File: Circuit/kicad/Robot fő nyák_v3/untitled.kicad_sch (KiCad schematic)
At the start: 4 parts, among them J13 Conn_01x06_Socket, J36 Conn_01x06_Socket, J37 Conn_01x06_Socket, J38 Conn_01x06_Socket

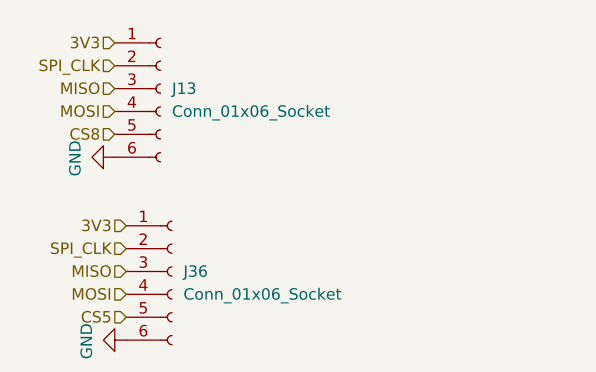
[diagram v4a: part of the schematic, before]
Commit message: kicad v0.1 footprint- assing spi finish
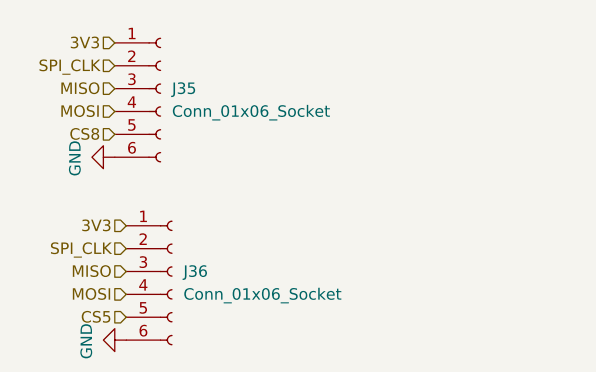
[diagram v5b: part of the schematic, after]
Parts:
- J35: renamed from J13; footprint (none) -> Connector_JST:JST_PH_B6B-PH-K_1x06_P2.00mm_Vertical
- J36, J37, J38: footprint (none) -> Connector_JST:JST_PH_B6B-PH-K_1x06_P2.00mm_Vertical
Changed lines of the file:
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@@
 			)
 		)
-		(property "Footprint" ""
+		(property "Footprint" "Connector_JST:JST_PH_B6B-PH-K_1x06_P2.00mm_Vertical"
 			(at 44.45 85.09 0)
 			(effects
@@
 		(on_board yes)
 		(dnp no)
-		(property "Reference" "#PWR016"
+		(property "Reference" "#PWR0124"
 			(at 33.02 92.71 0)
 			(effects
@@
 			(project "CM5IO"
 				(path "/e63e39d7-6ac0-4ffd-8aa3-1841a4541b55/a83afe30-5c7e-43cb-a5b2-f6f97a0812b3/86209e6a-92ae-4699-a125-02d46b525fc7"
-					(reference "#PWR016")
+					(reference "#PWR0124")
 					(unit 1)
 				)
@@
 		(on_board yes)
 		(dnp no)
-		(property "Reference" "#PWR015"
+		(property "Reference" "#PWR0123"
 			(at 31.75 73.66 0)
 			(effects
@@
 			(project "CM5IO"
 				(path "/e63e39d7-6ac0-4ffd-8aa3-1841a4541b55/a83afe30-5c7e-43cb-a5b2-f6f97a0812b3/86209e6a-92ae-4699-a125-02d46b525fc7"
-					(reference "#PWR015")
+					(reference "#PWR0123")
 					(unit 1)
 				)
@@
 			)
 		)
-		(property "Footprint" ""
+		(property "Footprint" "Connector_JST:JST_PH_B6B-PH-K_1x06_P2.00mm_Vertical"
 			(at 43.18 66.04 0)
 			(effects
@@
 			)
 		)
-		(property "Footprint" ""
+		(property "Footprint" "Connector_JST:JST_PH_B6B-PH-K_1x06_P2.00mm_Vertical"
 			(at 43.18 44.45 0)
 			(effects
@@
 		(dnp no)
 		(fields_autoplaced yes)
-		(property "Reference" "J13"
+		(property "Reference" "J35"
 			(at 43.18 24.1299 0)
 			(effects
@@
 			)
 		)
-		(property "Footprint" ""
+		(property "Footprint" "Connector_JST:JST_PH_B6B-PH-K_1x06_P2.00mm_Vertical"
 			(at 41.91 24.13 0)
 			(effects
@@
 			(project ""
 				(path "/e63e39d7-6ac0-4ffd-8aa3-1841a4541b55/a83afe30-5c7e-43cb-a5b2-f6f97a0812b3/86209e6a-92ae-4699-a125-02d46b525fc7"
-					(reference "J13")
+					(reference "J35")
 					(unit 1)
 				)
@@
 		(on_board yes)
 		(dnp no)
-		(property "Reference" "#PWR08"
+		(property "Reference" "#PWR0121"
 			(at 30.48 31.75 0)
 			(effects
@@
 			(project "CM5IO"
 				(path "/e63e39d7-6ac0-4ffd-8aa3-1841a4541b55/a83afe30-5c7e-43cb-a5b2-f6f97a0812b3/86209e6a-92ae-4699-a125-02d46b525fc7"
-					(reference "#PWR08")
+					(reference "#PWR0121")
 					(unit 1)
 				)
@@
 		(on_board yes)
 		(dnp no)
-		(property "Reference" "#PWR014"
+		(property "Reference" "#PWR0122"
 			(at 31.75 52.07 0)
 			(effects
@@
 			(project "CM5IO"
 				(path "/e63e39d7-6ac0-4ffd-8aa3-1841a4541b55/a83afe30-5c7e-43cb-a5b2-f6f97a0812b3/86209e6a-92ae-4699-a125-02d46b525fc7"
-					(reference "#PWR014")
-					(unit 1)
-				)
+					(reference "#PWR0122")
+					(unit 1)
+				)

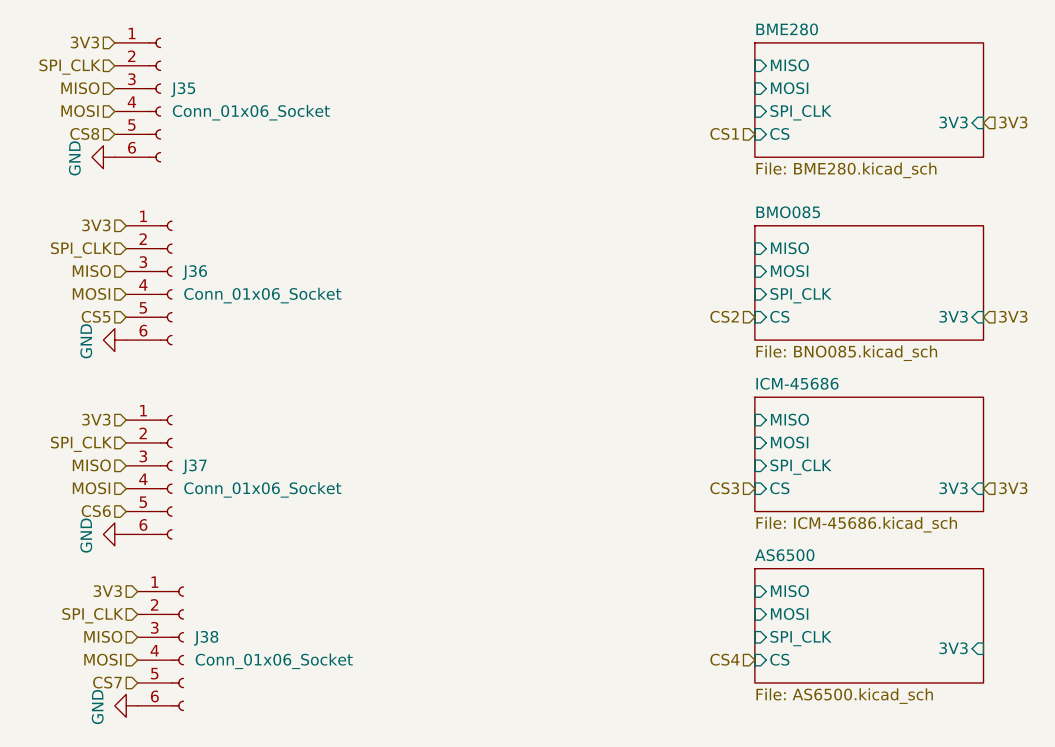
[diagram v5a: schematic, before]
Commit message: kicad  i2c and spi mux fixed and bugfixs
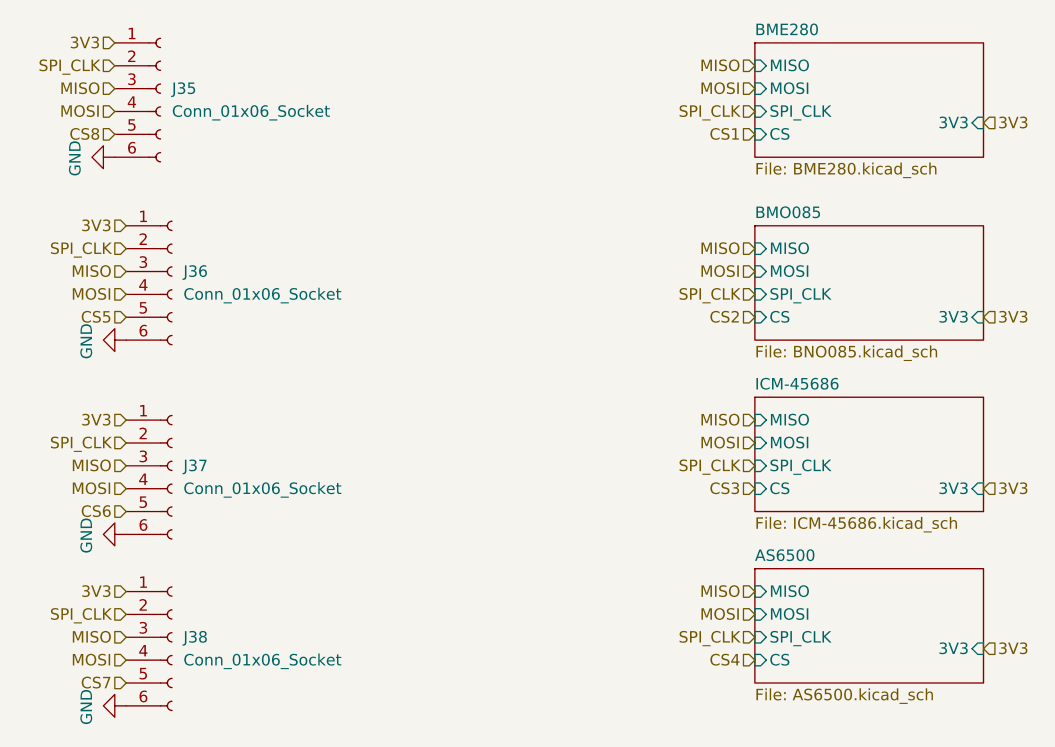
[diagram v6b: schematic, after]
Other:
- moved on the sheet: J38
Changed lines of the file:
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@@
 	(hierarchical_label "SPI_CLK"
 		(shape input)
-		(at 39.37 82.55 180)
+		(at 107.95 66.04 180)
+		(effects
+			(font
+				(size 1.27 1.27)
+			)
+			(justify right)
+		)
+	)
+	(hierarchical_label "MISO"
+		(shape input)
+		(at 107.95 60.96 180)
+		(effects
+			(font
+				(size 1.27 1.27)
+			)
+			(justify right)
+		)
+	)
+	(hierarchical_label "MOSI"
+		(shape input)
+		(at 107.95 63.5 180)
+		(effects
+			(font
+				(size 1.27 1.27)
+			)
+			(justify right)
+		)
+	)
+	(hierarchical_label "SPI_CLK"
+		(shape input)
+		(at 38.1 82.55 180)
 		(effects
 			(font
@@
 		)
 	)
+	(hierarchical_label "SPI_CLK"
+		(shape input)
+		(at 107.95 26.67 180)
+		(effects
+			(font
+				(size 1.27 1.27)
+			)
+			(justify right)
+		)
+	)
 	(hierarchical_label "MISO"
 		(shape input)
@@
 	(hierarchical_label "3V3"
 		(shape input)
+		(at 133.35 86.36 0)
+		(effects
+			(font
+				(size 1.27 1.27)
+			)
+			(justify left)
+		)
+	)
+	(hierarchical_label "3V3"
+		(shape input)
 		(at 133.35 68.58 0)
 		(effects
@@
 	(hierarchical_label "CS7"
 		(shape input)
-		(at 39.37 90.17 180)
+		(at 38.1 90.17 180)
+		(effects
+			(font
+				(size 1.27 1.27)
+			)
+			(justify right)
+		)
+	)
+	(hierarchical_label "SPI_CLK"
+		(shape input)
+		(at 107.95 46.99 180)
 		(effects
 			(font
@@
 		)
 	)
+	(hierarchical_label "MOSI"
+		(shape input)
+		(at 107.95 82.55 180)
+		(effects
+			(font
+				(size 1.27 1.27)
+			)
+			(justify right)
+		)
+	)
 	(hierarchical_label "CS1"
 		(shape input)
@@
 		)
 	)
+	(hierarchical_label "MISO"
+		(shape input)
+		(at 107.95 80.01 180)
+		(effects
+			(font
+				(size 1.27 1.27)
+			)
+			(justify right)
+		)
+	)
 	(hierarchical_label "CS8"
 		(shape input)
@@
 	(hierarchical_label "MISO"
 		(shape input)
-		(at 39.37 85.09 180)
+		(at 38.1 85.09 180)
 		(effects
 			(font
@@
 		)
 	)
+	(hierarchical_label "MOSI"
+		(shape input)
+		(at 107.95 44.45 180)
+		(effects
+			(font
+				(size 1.27 1.27)
+			)
+			(justify right)
+		)
+	)
+	(hierarchical_label "SPI_CLK"
+		(shape input)
+		(at 107.95 85.09 180)
+		(effects
+			(font
+				(size 1.27 1.27)
+			)
+			(justify right)
+		)
+	)
+	(hierarchical_label "MOSI"
+		(shape input)
+		(at 107.95 24.13 180)
+		(effects
+			(font
+				(size 1.27 1.27)
+			)
+			(justify right)
+		)
+	)
 	(hierarchical_label "3V3"
 		(shape input)
@@
 	(hierarchical_label "MISO"
 		(shape input)
+		(at 107.95 41.91 180)
+		(effects
+			(font
+				(size 1.27 1.27)
+			)
+			(justify right)
+		)
+	)
+	(hierarchical_label "MISO"
+		(shape input)
 		(at 38.1 44.45 180)
 		(effects
@@
 		)
 	)
+	(hierarchical_label "MISO"
+		(shape input)
+		(at 107.95 21.59 180)
+		(effects
+			(font
+				(size 1.27 1.27)
+			)
+			(justify right)
+		)
+	)
 	(hierarchical_label "SPI_CLK"
 		(shape input)
@@
 	(hierarchical_label "3V3"
 		(shape input)
-		(at 39.37 80.01 180)
-		(effects
-			(font
-				(size 1.27 1.27)
-			)
-			(justify right)
-		)
-	)
-	(hierarchical_label "MOSI"
-		(shape input)
-		(at 39.37 87.63 180)
+		(at 38.1 80.01 180)
+		(effects
+			(font
+				(size 1.27 1.27)
+			)
+			(justify right)
+		)
+	)
+	(hierarchical_label "MOSI"
+		(shape input)
+		(at 38.1 87.63 180)
 		(effects
 			(font
@@
 	(symbol
 		(lib_id "Connector:Conn_01x06_Socket")
-		(at 44.45 85.09 0)
+		(at 43.18 85.09 0)
 		(unit 1)
 		(exclude_from_sim no)
@@
 		(fields_autoplaced yes)
 		(property "Reference" "J38"
-			(at 45.72 85.0899 0)
+			(at 44.45 85.0899 0)
 			(effects
 				(font
@@
 		)
 		(property "Value" "Conn_01x06_Socket"
-			(at 45.72 87.6299 0)
+			(at 44.45 87.6299 0)
 			(effects
 				(font
@@
 		)
 		(property "Footprint" "Connector_JST:JST_PH_B6B-PH-K_1x06_P2.00mm_Vertical"
-			(at 44.45 85.09 0)
+			(at 43.18 85.09 0)
 			(effects
 				(font
@@
 		)
 		(property "Datasheet" "~"
-			(at 44.45 85.09 0)
+			(at 43.18 85.09 0)
 			(effects
 				(font
@@
 		)
 		(property "Description" "Generic connector, single row, 01x06, script generated"
-			(at 44.45 85.09 0)
+			(at 43.18 85.09 0)
 			(effects
 				(font
@@
 	(symbol
 		(lib_id "power:GND")
-		(at 39.37 92.71 270)
+		(at 38.1 92.71 270)
 		(unit 1)
 		(exclude_from_sim no)
@@
 		(dnp no)
 		(property "Reference" "#PWR0124"
-			(at 33.02 92.71 0)
+			(at 31.75 92.71 0)
 			(effects
 				(font
@@
 		)
 		(property "Value" "GND"
-			(at 34.9758 92.837 0)
+			(at 33.7058 92.837 0)
 			(effects
 				(font
@@
 		)
 		(property "Footprint" ""
-			(at 39.37 92.71 0)
+			(at 38.1 92.71 0)
 			(effects
 				(font
@@
 		)
 		(property "Datasheet" ""
-			(at 39.37 92.71 0)
+			(at 38.1 92.71 0)
 			(effects
 				(font
@@
 		)
 		(property "Description" "Power symbol creates a global label with name \"GND\" , ground"
-			(at 39.37 92.71 0)
-			(effects
-				(font
+			(at 38.1 92.71 0)
+			(effects
+				(font

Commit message: kicad update new readme media updates the circuit is 95% finished
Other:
- added sheet ADS8688 (ADS8688 .kicad_sch)
- moved on the sheet: J35, J36, J37, J38

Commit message: readme updated kicad circuit V1
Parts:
- renumbered J35 to SPI1, J38 to SPI2, J37 to SPI3, J36 to SPI4
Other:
- removed sheet AS6500
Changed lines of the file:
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@@
 		(dnp no)
 		(fields_autoplaced yes)
-		(property "Reference" "J38"
+		(property "Reference" "SPI2"
 			(at 44.45 46.9899 0)
 			(effects
@@
 			(project "CM5IO"
 				(path "/e63e39d7-6ac0-4ffd-8aa3-1841a4541b55/a83afe30-5c7e-43cb-a5b2-f6f97a0812b3/86209e6a-92ae-4699-a125-02d46b525fc7"
-					(reference "J38")
+					(reference "SPI2")
 					(unit 1)
 				)
@@
 		(on_board yes)
 		(dnp no)
-		(property "Reference" "#PWR0124"
+		(property "Reference" "#PWR0143"
 			(at 31.75 54.61 0)
 			(effects
@@
 			(project "CM5IO"
 				(path "/e63e39d7-6ac0-4ffd-8aa3-1841a4541b55/a83afe30-5c7e-43cb-a5b2-f6f97a0812b3/86209e6a-92ae-4699-a125-02d46b525fc7"
-					(reference "#PWR0124")
+					(reference "#PWR0143")
 					(unit 1)
 				)
@@
 		(on_board yes)
 		(dnp no)
-		(property "Reference" "#PWR0123"
+		(property "Reference" "#PWR0144"
 			(at 31.75 74.93 0)
 			(effects
@@
 			(project "CM5IO"
 				(path "/e63e39d7-6ac0-4ffd-8aa3-1841a4541b55/a83afe30-5c7e-43cb-a5b2-f6f97a0812b3/86209e6a-92ae-4699-a125-02d46b525fc7"
-					(reference "#PWR0123")
+					(reference "#PWR0144")
 					(unit 1)
 				)
@@
 		(dnp no)
 		(fields_autoplaced yes)
-		(property "Reference" "J37"
+		(property "Reference" "SPI3"
 			(at 44.45 67.3099 0)
 			(effects
@@
 			(project "CM5IO"
 				(path "/e63e39d7-6ac0-4ffd-8aa3-1841a4541b55/a83afe30-5c7e-43cb-a5b2-f6f97a0812b3/86209e6a-92ae-4699-a125-02d46b525fc7"
-					(reference "J37")
+					(reference "SPI3")
 					(unit 1)
 				)
@@
 		(dnp no)
 		(fields_autoplaced yes)
-		(property "Reference" "J36"
+		(property "Reference" "SPI4"
 			(at 44.45 86.3599 0)
 			(effects
@@
 			(project "CM5IO"
 				(path "/e63e39d7-6ac0-4ffd-8aa3-1841a4541b55/a83afe30-5c7e-43cb-a5b2-f6f97a0812b3/86209e6a-92ae-4699-a125-02d46b525fc7"
-					(reference "J36")
+					(reference "SPI4")
 					(unit 1)
 				)
@@
 		(dnp no)
 		(fields_autoplaced yes)
-		(property "Reference" "J35"
+		(property "Reference" "SPI1"
 			(at 44.45 26.6699 0)
 			(effects
@@
 			(project ""
 				(path "/e63e39d7-6ac0-4ffd-8aa3-1841a4541b55/a83afe30-5c7e-43cb-a5b2-f6f97a0812b3/86209e6a-92ae-4699-a125-02d46b525fc7"
-					(reference "J35")
+					(reference "SPI1")
 					(unit 1)
 				)
@@
 		(on_board yes)
 		(dnp no)
-		(property "Reference" "#PWR0121"
+		(property "Reference" "#PWR0142"
 			(at 31.75 34.29 0)
 			(effects
@@
 			(project "CM5IO"
 				(path "/e63e39d7-6ac0-4ffd-8aa3-1841a4541b55/a83afe30-5c7e-43cb-a5b2-f6f97a0812b3/86209e6a-92ae-4699-a125-02d46b525fc7"
-					(reference "#PWR0121")
+					(reference "#PWR0142")
 					(unit 1)
 				)
@@
 		(on_board yes)
 		(dnp no)
-		(property "Reference" "#PWR0122"
+		(property "Reference" "#PWR0145"
 			(at 31.75 93.98 0)
 			(effects
@@
 			(project "CM5IO"
 				(path "/e63e39d7-6ac0-4ffd-8aa3-1841a4541b55/a83afe30-5c7e-43cb-a5b2-f6f97a0812b3/86209e6a-92ae-4699-a125-02d46b525fc7"
-					(reference "#PWR0122")
+					(reference "#PWR0145")
 					(unit 1)
 				)
@@
 				)
 			)
-		)
-	)
-	(sheet
-		(at 162.56 82.55)
-		(size 25.4 12.7)
-		(exclude_from_sim yes)
-		(in_bom no)
-		(on_board no)
-		(dnp yes)
-		(fields_autoplaced yes)
-		(stroke
-			(width 0.1524)
-			(type solid)
-		)
-		(fill
-			(color 0 0 0 0.0000)
-		)
-		(property "Sheetname" "AS6500"
-			(at 162.56 81.8384 0)
-			(effects
-				(font
-					(size 1.27 1.27)
-				)
-				(justify left bottom)
-			)
-		)
-		(property "Sheetfile" "AS6500.kicad_sch"
-			(at 162.56 95.8346 0)
-			(effects
-				(font
-					(size 1.27 1.27)
-				)
-				(justify left top)
-			)
-		)
-		(pin "3V3" input
-			(at 187.96 91.44 0)
-			(effects
-				(font
-					(size 1.27 1.27)
-				)
-				(justify right)
-			)
-		)
-		(pin "CS" input
-			(at 162.56 92.71 180)
-			(effects
-				(font
-					(size 1.27 1.27)
-				)
-				(justify left)
-			)
-		)
-		(pin "MISO" input
-			(at 162.56 85.09 180)
-			(effects
-				(font
-					(size 1.27 1.27)
-				)
-				(justify left)
-			)
-		)
-		(pin "MOSI" input
-			(at 162.56 87.63 180)
-			(effects
-				(font
-					(size 1.27 1.27)
-				)
-				(justify left)
-			)
-		)
-		(pin "SPI_CLK" input
-			(at 162.56 90.17 180)
-			(effects
-				(font
-					(size 1.27 1.27)
-				)
-				(justify left)
-			)
-		)
-		(instances
-			(project "CM5IO"
-				(path "/e63e39d7-6ac0-4ffd-8aa3-1841a4541b55/a83afe30-5c7e-43cb-a5b2-f6f97a0812b3/86209e6a-92ae-4699-a125-02d46b525fc7"
-					(page "18")
-				)
-			)
